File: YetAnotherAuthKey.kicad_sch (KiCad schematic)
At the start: 31 parts, among them P1 USB_C_Plug_USB2.0, SW1 SW_Push, U1 RP2350_60QFN, U2 MCP1700x-330xxTT, Y1 ABM8-272-T3

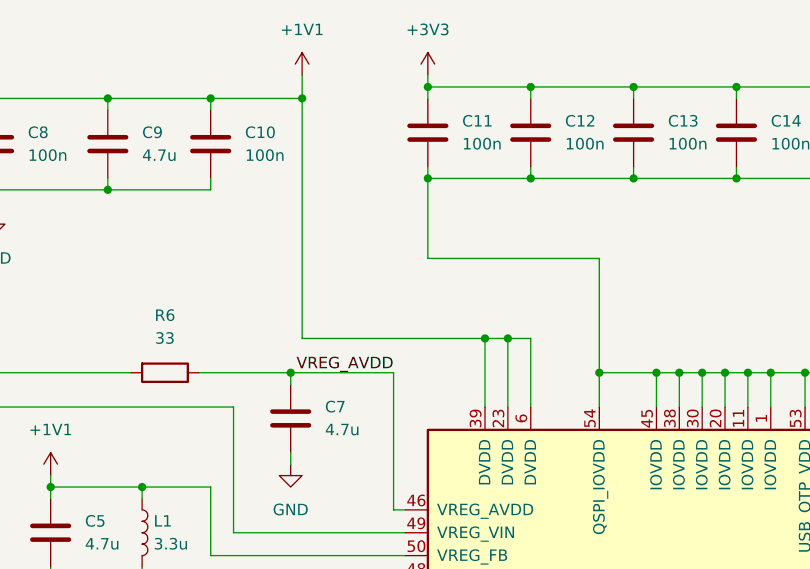
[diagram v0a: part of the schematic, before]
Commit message: clean schematic
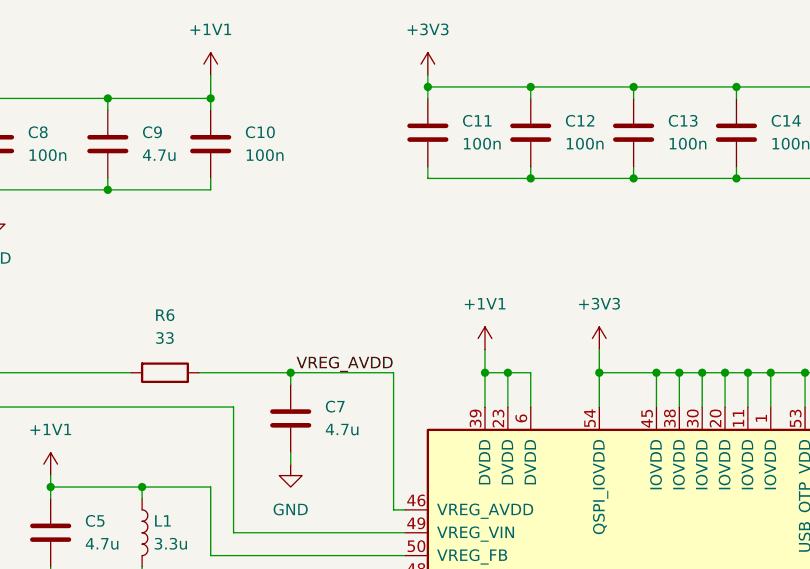
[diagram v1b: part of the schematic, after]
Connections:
- net +3V3: now also U1.1 (IOVDD), U1.11 (IOVDD), U1.20 (IOVDD), U1.30 (IOVDD), U1.38 (IOVDD), U1.44 (ADC_AVDD), U1.45 (IOVDD), U1.53 (USB_OTP_VDD), U1.54 (QSPI_IOVDD)
- net GND: no longer U1.1 (IOVDD), U1.11 (IOVDD), U1.20 (IOVDD), U1.30 (IOVDD), U1.38 (IOVDD), U1.44 (ADC_AVDD), U1.45 (IOVDD), U1.53 (USB_OTP_VDD), U1.54 (QSPI_IOVDD)
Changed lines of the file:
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@@
 	)
 	(junction
-		(at 180.34 30.48)
-		(diameter 0)
-		(color 0 0 0 0)
-	)
-	(junction
 		(at 260.35 20.32)
 		(diameter 0)
@@
 	)
 	(junction
-		(at 186.69 48.26)
-		(diameter 0)
-		(color 0 0 0 0)
-	)
-	(junction
 		(at 237.49 20.32)
 		(diameter 0)
@@
 	)
 	(junction
-		(at 166.37 21.59)
-		(diameter 0)
-		(color 0 0 0 0)
-	)
-	(junction
 		(at 226.06 30.48)
 		(diameter 0)
@@
 	)
 	(junction
-		(at 189.23 48.26)
+		(at 189.23 52.07)
 		(diameter 0)
 		(color 0 0 0 0)
@@
 	)
 	(junction
+		(at 199.39 52.07)
+		(diameter 0)
+		(color 0 0 0 0)
+	)
+	(junction
 		(at 144.78 21.59)
 		(diameter 0)
@@
 	)
 	(junction
-		(at 237.49 30.48)
+		(at 186.69 52.07)
 		(diameter 0)
 		(color 0 0 0 0)
 	)
 	(junction
-		(at 85.09 46.99)
+		(at 237.49 30.48)
 		(diameter 0)
 		(color 0 0 0 0)
 	)
 	(junction
-		(at 148.59 64.77)
+		(at 85.09 46.99)
 		(diameter 0)
 		(color 0 0 0 0)
 	)
 	(junction
-		(at 50.8 101.6)
+		(at 148.59 64.77)
 		(diameter 0)
 		(color 0 0 0 0)
 	)
 	(junction
-		(at 199.39 52.07)
+		(at 50.8 101.6)
 		(diameter 0)
 		(color 0 0 0 0)
@@
 	(wire
 		(pts
-			(xy 166.37 19.05) (xy 166.37 21.59)
+			(xy 156.21 19.05) (xy 156.21 21.59)
 		)
 		(stroke
@@
 	(wire
 		(pts
+			(xy 199.39 49.53) (xy 199.39 52.07)
+		)
+		(stroke
+			(width 0)
+			(type default)
+		)
+	)
+	(wire
+		(pts
 			(xy 237.49 30.48) (xy 237.49 29.21)
 		)
@@
 	(wire
 		(pts
-			(xy 180.34 39.37) (xy 180.34 30.48)
-		)
-		(stroke
-			(width 0)
-			(type default)
-		)
-	)
-	(wire
-		(pts
 			(xy 205.74 52.07) (xy 199.39 52.07)
 		)
@@
 	(wire
 		(pts
-			(xy 191.77 48.26) (xy 191.77 55.88)
+			(xy 191.77 52.07) (xy 191.77 55.88)
 		)
 		(stroke
@@
 	(wire
 		(pts
-			(xy 189.23 48.26) (xy 189.23 55.88)
+			(xy 189.23 52.07) (xy 189.23 55.88)
 		)
 		(stroke
@@
 	(wire
 		(pts
-			(xy 210.82 52.07) (xy 210.82 55.88)
+			(xy 186.69 49.53) (xy 186.69 52.07)
 		)
 		(stroke
@@
 	(wire
 		(pts
-			(xy 132.08 31.75) (xy 144.78 31.75)
+			(xy 210.82 52.07) (xy 210.82 55.88)
 		)
 		(stroke
@@
 	(wire
 		(pts
-			(xy 248.92 30.48) (xy 248.92 29.21)
+			(xy 132.08 31.75) (xy 144.78 31.75)
 		)
 		(stroke
@@
 	(wire
 		(pts
-			(xy 248.92 20.32) (xy 248.92 21.59)
+			(xy 248.92 30.48) (xy 248.92 29.21)
 		)
 		(stroke
@@
 	(wire
 		(pts
-			(xy 255.27 58.42) (xy 267.97 58.42)
+			(xy 248.92 20.32) (xy 248.92 21.59)
 		)
 		(stroke
@@
 	(wire
 		(pts
-			(xy 158.75 69.85) (xy 177.8 69.85)
+			(xy 255.27 58.42) (xy 267.97 58.42)
 		)
 		(stroke
@@
 	(wire
 		(pts
-			(xy 53.34 31.75) (xy 53.34 34.29)
+			(xy 158.75 69.85) (xy 177.8 69.85)
 		)
 		(stroke
@@
 	(wire
 		(pts
-			(xy 214.63 20.32) (xy 226.06 20.32)
+			(xy 53.34 31.75) (xy 53.34 34.29)
 		)
 		(stroke
@@
 	(wire
 		(pts
-			(xy 156.21 21.59) (xy 166.37 21.59)
+			(xy 214.63 20.32) (xy 226.06 20.32)
 		)
 		(stroke
@@
 	(wire
 		(pts
-			(xy 166.37 21.59) (xy 166.37 48.26)
-		)
-		(stroke
-			(width 0)
-			(type default)
-		)
-	)
-	(wire
-		(pts
-			(xy 166.37 48.26) (xy 186.69 48.26)
-		)
-		(stroke
-			(width 0)
-			(type default)
-		)
-	)
-	(wire
-		(pts
-			(xy 186.69 48.26) (xy 189.23 48.26)
+			(xy 186.69 52.07) (xy 189.23 52.07)
 		)
 		(stroke
@@
 	(wire
 		(pts
-			(xy 199.39 39.37) (xy 180.34 39.37)
-		)
-		(stroke
-			(width 0)
-			(type default)
-		)
-	)
-	(wire
-		(pts
 			(xy 241.3 66.04) (xy 247.65 66.04)
 		)
@@
 	(wire
 		(pts
-			(xy 186.69 48.26) (xy 186.69 55.88)
+			(xy 186.69 52.07) (xy 186.69 55.88)
 		)
 		(stroke
@@
 	(wire
 		(pts
-			(xy 189.23 48.26) (xy 191.77 48.26)
+			(xy 189.23 52.07) (xy 191.77 52.07)
 		)
 		(stroke
@@
 	(wire
 		(pts
-			(xy 199.39 39.37) (xy 199.39 52.07)
-		)
-		(stroke
-			(width 0)
-			(type default)
-		)
-	)
-	(wire
-		(pts
 			(xy 222.25 52.07) (xy 218.44 52.07)
 		)
@@
 	)
 	(symbol
+		(lib_id "power:+1V1")
+		(at 186.69 49.53 0)
+		(unit 1)
+		(exclude_from_sim no)
+		(in_bom yes)
+		(on_board yes)
+		(dnp no)
+		(fields_autoplaced yes)
+		(property "Reference" "#PWR06"
+			(at 186.69 53.34 0)
+			(effects
+				(font
+					(size 1.27 1.27)
+				)
+				(hide yes)
+			)
+		)
+		(property "Value" "+1V1"
+			(at 186.69 44.45 0)
+			(effects
+				(font
+					(size 1.27 1.27)
+				)
+			)
+		)
+		(property "Footprint" ""
+			(at 186.69 49.53 0)
+			(effects
+				(font
+					(size 1.27 1.27)
+				)
+				(hide yes)
+			)
+		)
+		(property "Datasheet" ""
+			(at 186.69 49.53 0)
+			(effects
+				(font
+					(size 1.27 1.27)
+				)
+				(hide yes)
+			)
+		)
+		(property "Description" "Power symbol creates a global label with name \"+1V1\""
+			(at 186.69 49.53 0)
+			(effects
+				(font
+					(size 1.27 1.27)
+				)
+				(hide yes)
+			)
+		)
+		(pin "1"
+		)
+		(instances
+			(project ""
+				(path "/7a7470a0-a250-4187-9aed-176069ab6ef6"
+					(reference "#PWR06")
+					(unit 1)
+				)
+			)
+		)
+	)
+	(symbol
 		(lib_id "Device:C")
 		(at 100.33 39.37 0)
@@
 	)
 	(symbol
+		(lib_id "power:+3V3")
+		(at 199.39 49.53 0)
+		(unit 1)
+		(exclude_from_sim no)
+		(in_bom yes)
+		(on_board yes)
+		(dnp no)
+		(fields_autoplaced yes)
+		(property "Reference" "#PWR05"
+			(at 199.39 53.34 0)
+			(effects
+				(font
+					(size 1.27 1.27)
+				)
+				(hide yes)
+			)
+		)
+		(property "Value" "+3V3"
+			(at 199.39 44.45 0)
+			(effects
+				(font
+					(size 1.27 1.27)
+				)
+			)
+		)
+		(property "Footprint" ""
+			(at 199.39 49.53 0)
+			(effects
+				(font
+					(size 1.27 1.27)
+				)
+				(hide yes)
+			)
+		)
+		(property "Datasheet" ""
+			(at 199.39 49.53 0)
+			(effects
+				(font
+					(size 1.27 1.27)
+				)
+				(hide yes)
+			)
+		)
+		(property "Description" "Power symbol creates a global label with name \"+3V3\""
+			(at 199.39 49.53 0)
+			(effects
+				(font
+					(size 1.27 1.27)
+				)
+				(hide yes)
+			)
+		)
+		(pin "1"
+		)
+		(instances
+			(project ""
+				(path "/7a7470a0-a250-4187-9aed-176069ab6ef6"
+					(reference "#PWR05")
+					(unit 1)
+				)
+			)
+		)
+	)
+	(symbol
 		(lib_id "power:GND")
 		(at 271.78 33.02 0)
@@
 	(symbol
 		(lib_id "power:+1V1")
-		(at 166.37 19.05 0)
+		(at 156.21 19.05 0)
 		(unit 1)
 		(exclude_from_sim no)
@@
 		(fields_autoplaced yes)
 		(property "Reference" "#PWR018"
-			(at 166.37 22.86 0)
+			(at 156.21 22.86 0)
 			(effects
 				(font
@@
 		)
 		(property "Value" "+1V1"
-			(at 166.37 13.97 0)
+			(at 156.21 13.97 0)
 			(effects
 				(font
@@
 		)
 		(property "Footprint" ""
-			(at 166.37 19.05 0)
+			(at 156.21 19.05 0)
 			(effects
 				(font
@@
 		)
 		(property "Datasheet" ""
-			(at 166.37 19.05 0)
+			(at 156.21 19.05 0)
 			(effects
 				(font
@@
 		)
 		(property "Description" "Power symbol creates a global label with name \"+1V1\""
-			(at 166.37 19.05 0)
+			(at 156.21 19.05 0)
 			(effects
 				(font

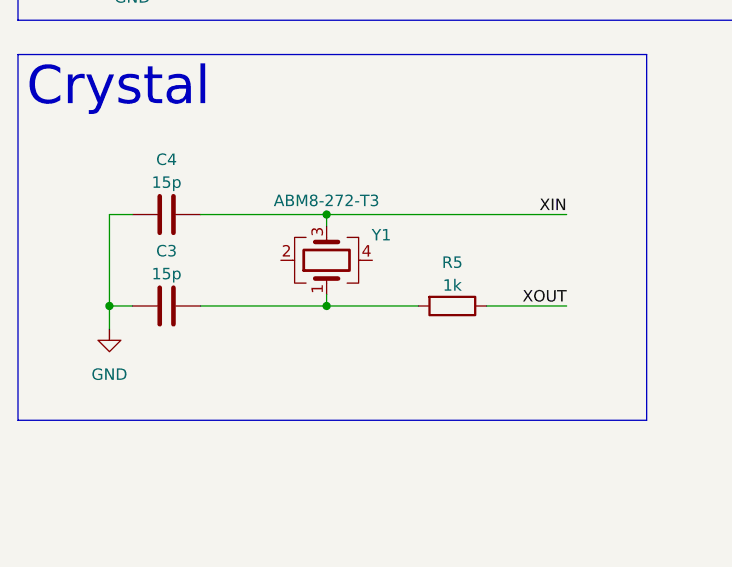
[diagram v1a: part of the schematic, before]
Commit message: add missing grounds
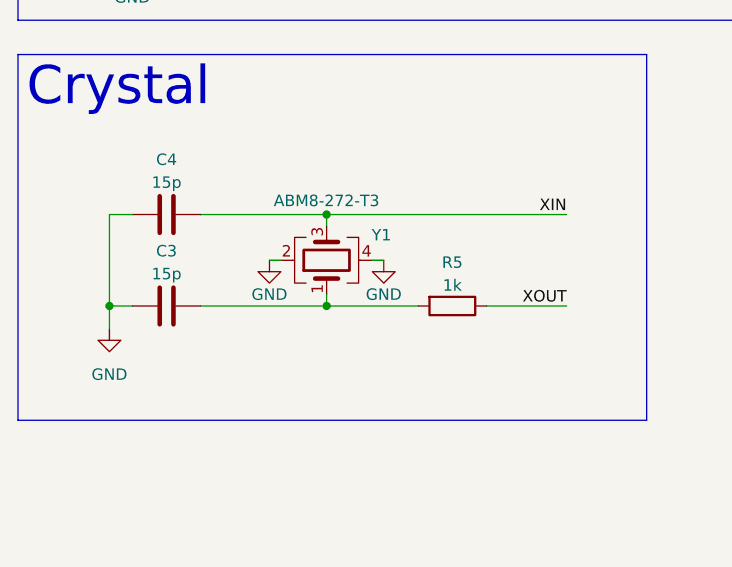
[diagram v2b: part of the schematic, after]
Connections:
- net GND: now also Y1.2, Y1.4
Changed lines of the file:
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@@
 	(wire
 		(pts
+			(xy 57.15 106.68) (xy 55.88 106.68)
+		)
+		(stroke
+			(width 0)
+			(type default)
+		)
+	)
+	(wire
+		(pts
 			(xy 132.08 22.86) (xy 132.08 21.59)
 		)
@@
 	(wire
 		(pts
+			(xy 44.45 106.68) (xy 45.72 106.68)
+		)
+		(stroke
+			(width 0)
+			(type default)
+		)
+	)
+	(wire
+		(pts
 			(xy 199.39 52.07) (xy 199.39 55.88)
 		)
@@
 	)
 	(symbol
+		(lib_id "power:GND")
+		(at 44.45 106.68 0)
+		(unit 1)
+		(exclude_from_sim no)
+		(in_bom yes)
+		(on_board yes)
+		(dnp no)
+		(property "Reference" "#PWR012"
+			(at 44.45 113.03 0)
+			(effects
+				(font
+					(size 1.27 1.27)
+				)
+				(hide yes)
+			)
+		)
+		(property "Value" "GND"
+			(at 44.45 110.49 0)
+			(effects
+				(font
+					(size 1.27 1.27)
+				)
+			)
+		)
+		(property "Footprint" ""
+			(at 44.45 106.68 0)
+			(effects
+				(font
+					(size 1.27 1.27)
+				)
+				(hide yes)
+			)
+		)
+		(property "Datasheet" ""
+			(at 44.45 106.68 0)
+			(effects
+				(font
+					(size 1.27 1.27)
+				)
+				(hide yes)
+			)
+		)
+		(property "Description" "Power symbol creates a global label with name \"GND\" , ground"
+			(at 44.45 106.68 0)
+			(effects
+				(font
+					(size 1.27 1.27)
+				)
+				(hide yes)
+			)
+		)
+		(pin "1"
+		)
+		(instances
+			(project ""
+				(path "/7a7470a0-a250-4187-9aed-176069ab6ef6"
+					(reference "#PWR012")
+					(unit 1)
+				)
+			)
+		)
+	)
+	(symbol
 		(lib_id "Device:C")
 		(at 132.08 26.67 0)
@@
 					(unit 1)
 				)
+			)
+		)
+	)
+	(symbol
+		(lib_id "power:GND")
+		(at 57.15 106.68 0)
+		(unit 1)
+		(exclude_from_sim no)
+		(in_bom yes)
+		(on_board yes)
+		(dnp no)
+		(property "Reference" "#PWR013"
+			(at 57.15 113.03 0)
+			(effects
+				(font
+					(size 1.27 1.27)
+				)
+				(hide yes)
+			)
+		)
+		(property "Value" "GND"
+			(at 57.15 110.49 0)
+			(effects
+				(font
+					(size 1.27 1.27)
+				)
+			)
+		)
+		(property "Footprint" ""
+			(at 57.15 106.68 0)
+			(effects
+				(font
+					(size 1.27 1.27)
+				)
+				(hide yes)
+			)
+		)
+		(property "Datasheet" ""
+			(at 57.15 106.68 0)
+			(effects
+				(font
+					(size 1.27 1.27)
+				)
+				(hide yes)
+			)
+		)
+		(property "Description" "Power symbol creates a global label with name \"GND\" , ground"
+			(at 57.15 106.68 0)
+			(effects
+				(font
+					(size 1.27 1.27)
+				)
+				(hide yes)
+			)
+		)
+		(pin "1"
+		)
+		(instances
+			(project ""
+				(path "/7a7470a0-a250-4187-9aed-176069ab6ef6"
+					(reference "#PWR013")
+					(unit 1)
+				)

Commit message: finish pcb
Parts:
- removed P1: USB_C_Plug_USB2.0, Connector_USB:USB_C_Plug_Molex_105444, symbol Connector:USB_C_Plug_USB2.0
- removed R1: 5.1K, Resistor_SMD:R_0402_1005Metric, symbol Device:R
- added J1: USB_A, Connector_USB:USB_A_Molex_48037-2200_Horizontal, symbol Connector:USB_A
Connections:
- net GND: now also J1.4 (GND), J1.5 (Shield)
- net USB_D+: now also J1.3 (D+)
- net USB_D-: now also J1.2 (D-)
- net VBUS: now also J1.1 (VBUS)
- no-connect marks 39 -> 38
